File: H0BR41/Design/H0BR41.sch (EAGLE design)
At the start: 26 parts, among them P1 HEXABIT_17.32, U1 STM32G0B1CEU6NUFQFPN48_STM32_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, U2 LSM6DS3TR-C, U3 STMICROELECTRONICS_LSM303AGRT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, X1 8MH

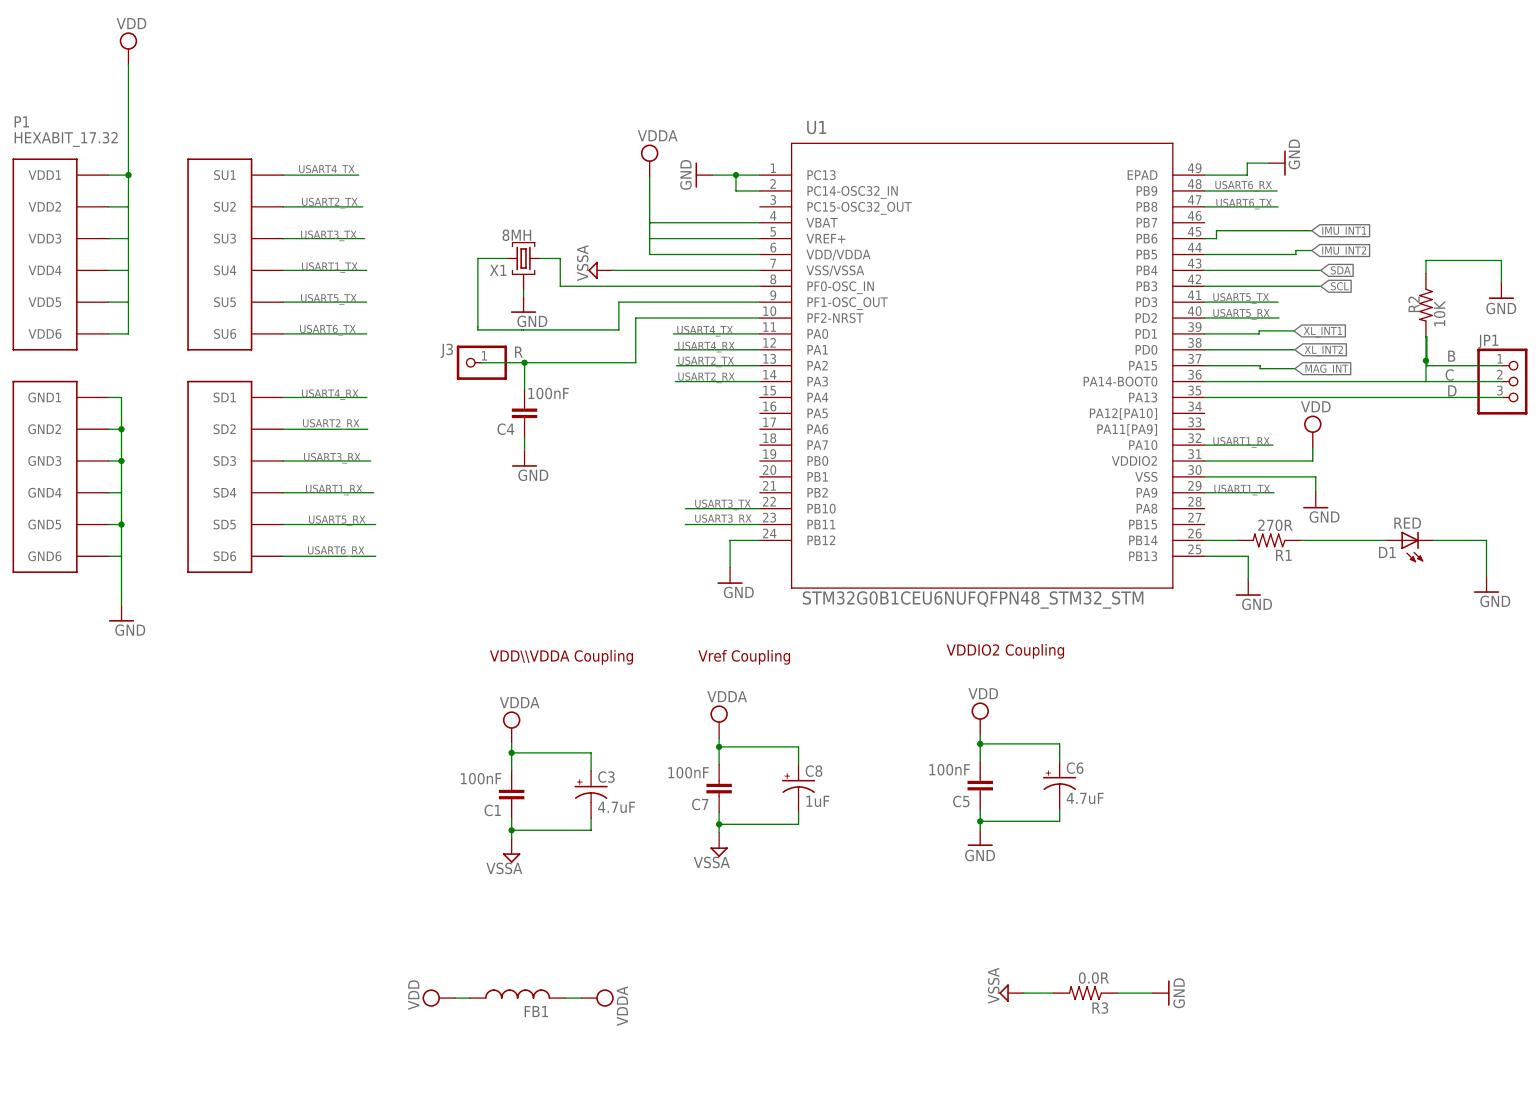
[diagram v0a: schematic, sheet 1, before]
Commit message: -Changing the layout to be like of master design in terms of the position of sensors ICs . -Changing the Schematic as well
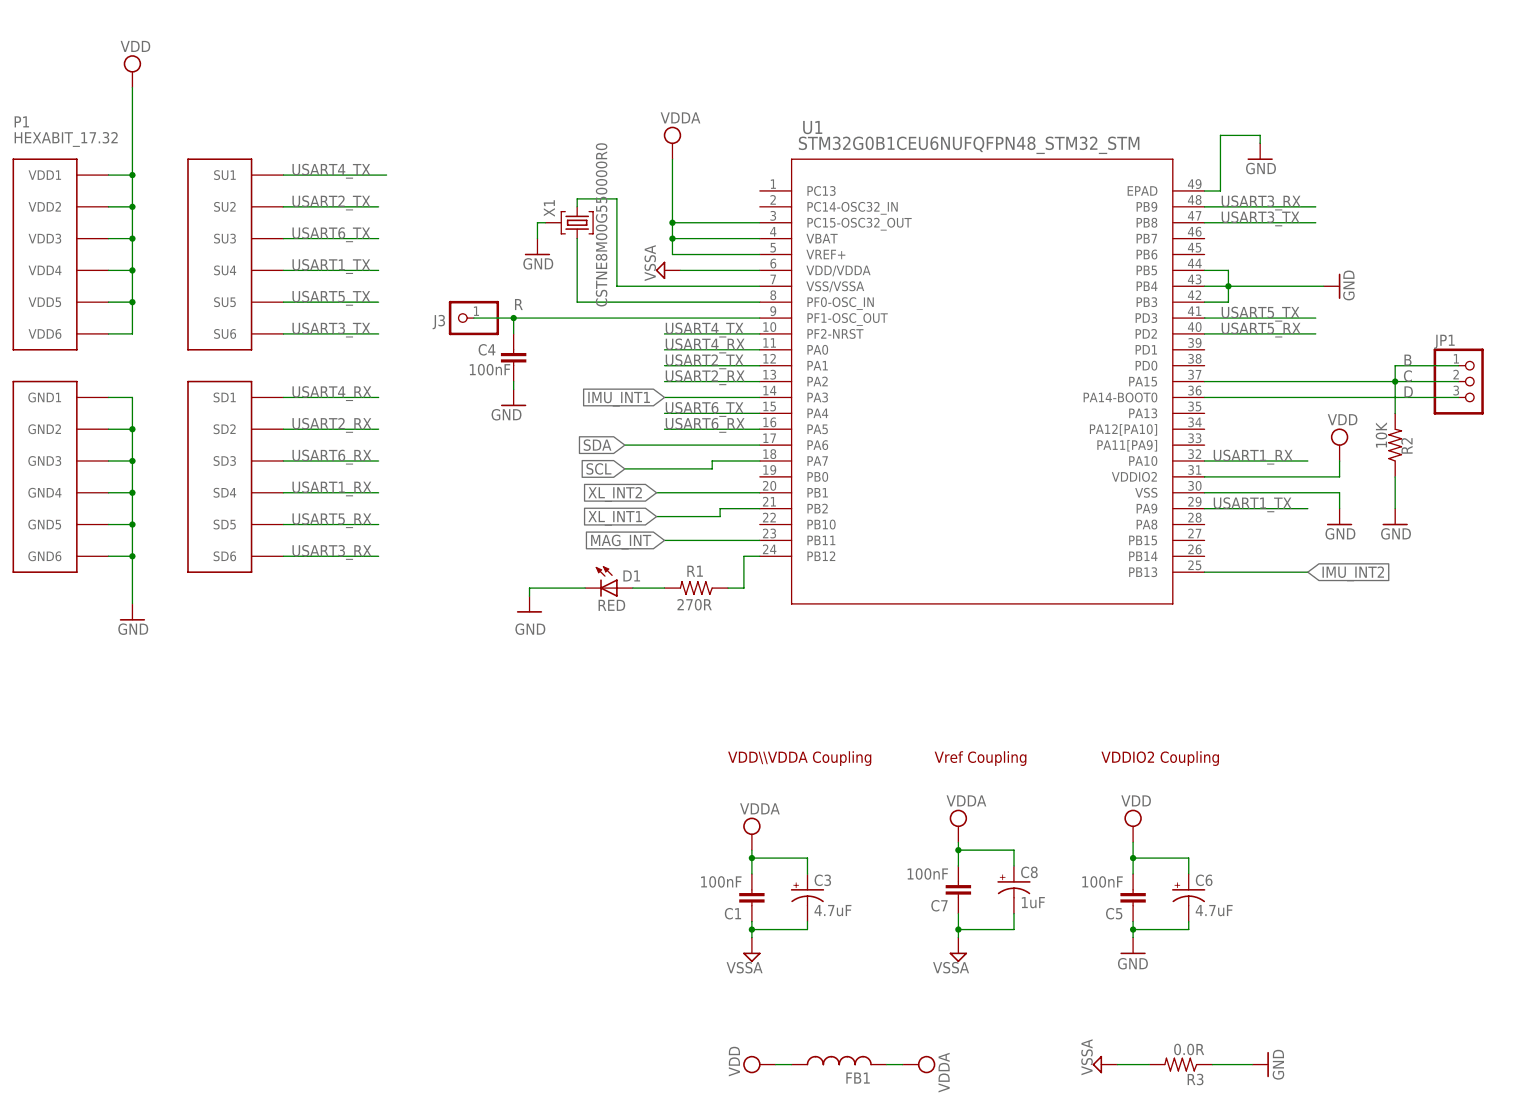
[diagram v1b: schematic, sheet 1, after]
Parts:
- U1: OCTOPART_URL https://octopart.com/stm32g0b1ceu6n-stmicroelectronics-1163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 -> (none)
- X1: value 8MH -> CSTNE8M00G550000R0
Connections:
- removed net N$17: R1.2, U1.PB14
- removed net N$19: D1.A, R1.1
- removed net N$2 (its old number): U1.PF1-OSC_OUT, X1.1
- new net N$1: R1.1, U1.PB12
- new net N$4: D1.A, R1.2
- new net N$5: U1.VSS/VSSA, X1.1
- net C: now also U1.PA15; no longer U1.PA14-BOOT0
- net D: now also U1.PA14-BOOT0; no longer U1.PA13
- net GND: now also U1.PB3, U1.PB4, U1.PB5; no longer U1.PB12, U1.PB13, U1.PC13, U1.PC14-OSC32_IN
- net GND1: now also U1.VDD/VDDA; no longer U1.VSS/VSSA
- net IMU_INT1: now also U1.PA3; no longer U1.PB6
- net IMU_INT2: now also U1.PB13; no longer U1.PB5
- net MAG_INT: now also U1.PB11; no longer U1.PA15
- net R: now also U1.PF1-OSC_OUT; no longer U1.PF2-NRST
- net SCL: now also R8.2, U1.PA7; no longer R9.2, U1.PB3
- net SDA: now also R9.2, U1.PA6; no longer R8.2, U1.PB4
- net USART2_RX: now also U1.PA2; no longer U1.PA3
- net USART2_TX: now also U1.PA1; no longer U1.PA2
- net USART3_RX: now also P1.SD6, U1.PB9; no longer P1.SD3, U1.PB11
- net USART3_TX: now also P1.SU6, U1.PB8; no longer P1.SU3, U1.PB10
- net USART4_RX: now also U1.PA0; no longer U1.PA1
- net USART4_TX: now also U1.PF2-NRST; no longer U1.PA0
- net USART6_RX: now also P1.SD3, U1.PA5; no longer P1.SD6, U1.PB9
- net USART6_TX: now also P1.SU3, U1.PA4; no longer P1.SU6, U1.PB8
- net VCC: now also U1.PC15-OSC32_OUT; no longer U1.VDD/VDDA
- net XL_INT1: now also U1.PB2; no longer U1.PD1
- net XL_INT2: now also U1.PB1; no longer U1.PD0
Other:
- note added: "Ibrahim Zaeiter"
- note removed: "Esraa Alkadour"
- moved on the sheet: C1, C12, C13, C14, C15, C3, C4, C5, C6, C7, C8, C9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

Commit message: -Correcting some fault connections
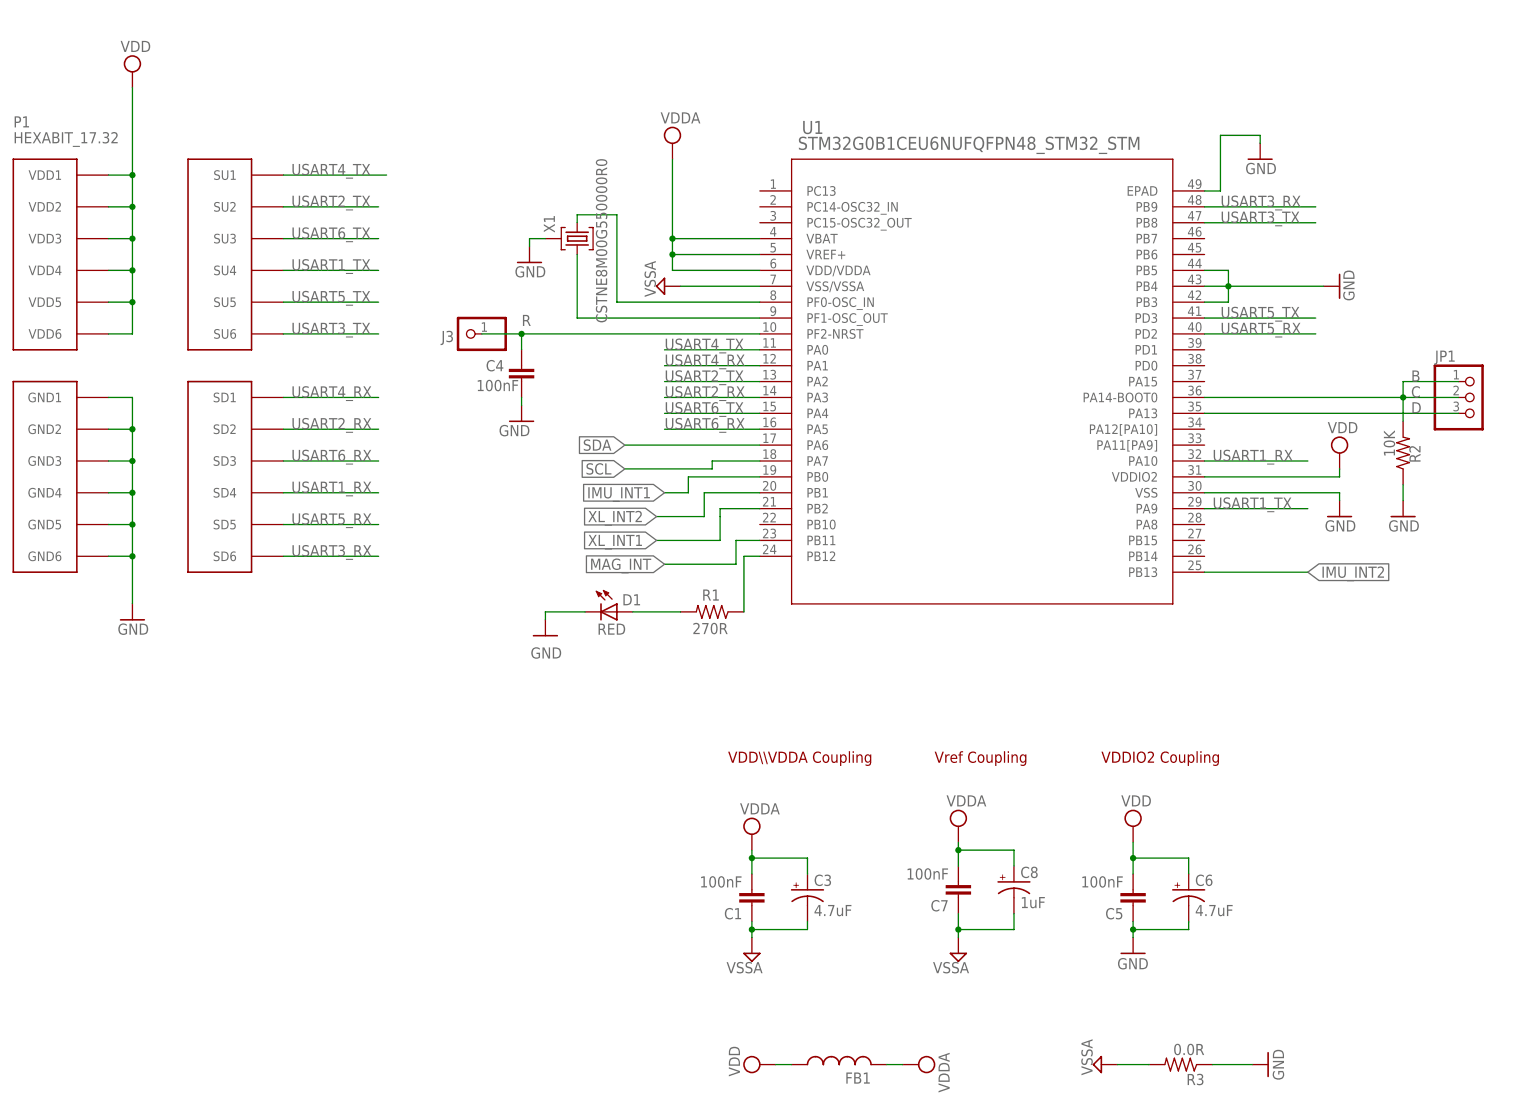
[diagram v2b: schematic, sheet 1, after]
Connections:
- net C: now also U1.PA14-BOOT0; no longer U1.PA15
- net D: now also U1.PA13; no longer U1.PA14-BOOT0
- net GND1: now also U1.VSS/VSSA; no longer U1.VDD/VDDA
- net IMU_INT1: now also U1.PB0; no longer U1.PA3
- net N$3: now also U1.PF1-OSC_OUT; no longer U1.PF0-OSC_IN
- net N$5: now also U1.PF0-OSC_IN; no longer U1.VSS/VSSA
- net R: now also U1.PF2-NRST; no longer U1.PF1-OSC_OUT
- net USART2_RX: now also U1.PA3; no longer U1.PA2
- net USART2_TX: now also U1.PA2; no longer U1.PA1
- net USART4_RX: now also U1.PA1; no longer U1.PA0
- net USART4_TX: now also U1.PA0; no longer U1.PF2-NRST
- net VCC: now also U1.VDD/VDDA; no longer U1.PC15-OSC32_OUT
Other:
- note added: "I2C2"
- moved on the sheet: C4, D1, J3, JP1, R1, R2, X1

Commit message: -Correcting some issues related to part names
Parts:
- removed C15, C5: 100nF, HEXABITZ_RCLS:C-0603
- removed C9: 220nF, HEXABITZ_RCLS:C-0805-POL
- added C10, C11: 100nF, HEXABITZ_RCLS:C-0603
- added C2: 1uF, HEXABITZ_RCLS:C-0805-POL
- C14: value 100nF -> 220nF; device HEXABITZ_RCLS:C-0603 -> HEXABITZ_RCLS:C-0805-POL; CAPACITANCE 100nF -> 4.7uF; MFN AVX CORPORATION -> KEMET; MPN '0603YC104K4T2A -> C0805C224K1RACTU; OCTOPART_URL 'https://octopart.com/0603yc104k4t2a-avx+interconnect+%2F+e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 -> https://octopart.com/c0805c224k1ractu-kemet-12818106?r=sp; TOLERANCE 10% -> 20%; VOLTAGE_RATING 16.0 V -> 10.0 V
- C4: value 100nF -> 4.7uF; device HEXABITZ_RCLS:C-0603 -> HEXABITZ_RCLS:C-0805-POL; CAPACITANCE 100nF -> 4.7uF; MFN AVX CORPORATION -> Panasonic; MPN '0603YC104K4T2A -> 10TPU4R7MSI; OCTOPART_URL 'https://octopart.com/0603yc104k4t2a-avx+interconnect+%2F+e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 -> https://octopart.com/10tpu4r7msi-panasonic-29487748; TOLERANCE 10% -> 20%; VOLTAGE_RATING 16.0 V -> 10.0 V
- C6: value 4.7uF -> 100nF; device HEXABITZ_RCLS:C-0805-POL -> HEXABITZ_RCLS:C-0603; CAPACITANCE 4.7uF -> 100nF; MFN Panasonic -> AVX CORPORATION; MPN 10TPU4R7MSI -> '0603YC104K4T2A; OCTOPART_URL https://octopart.com/10tpu4r7msi-panasonic-29487748 -> 'https://octopart.com/0603yc104k4t2a-avx+interconnect+%2F+e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; TOLERANCE 20% -> 10%; VOLTAGE_RATING 10.0 V -> 16.0 V
- C8: value 1uF -> 100nF; device HEXABITZ_RCLS:C-0805-POL -> HEXABITZ_RCLS:C-0603; CAPACITANCE 1.00uF -> 100nF; MFN 'YAGEO [VA] -> AVX CORPORATION; MPN 'CC0805KKX7R7BB105 -> '0603YC104K4T2A; OCTOPART_URL https://octopart.com/cc0805kkx7r7bb105-yageo-8376555?r=sp -> 'https://octopart.com/0603yc104k4t2a-avx+interconnect+%2F+e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
- renumbered R8 to R5, R9 to R4
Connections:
- net GND: now also C1.1, C10.1, C11.1, C14.-, C4.-, C8.1; no longer C14.1, C15.1, C4.1, C5.1, C6.-, C9.-
- net GND1: now also C2.-, C6.1; no longer C1.1, C8.-
- net N$2: now also C14.+; no longer C9.+
- net R: now also C1.2; no longer C4.2
- net VCC: now also C2.+, C6.2; no longer C1.2, C8.+
- net VDD: now also C10.2, C11.2, C4.+, C8.2; no longer C14.2, C15.2, C5.2, C6.+
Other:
- moved on the sheet: C1, C12, C13
